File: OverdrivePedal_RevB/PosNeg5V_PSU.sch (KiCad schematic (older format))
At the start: 11 parts, among them U3 TPS60400, U7 SE8233X2, U8 SE8250X2

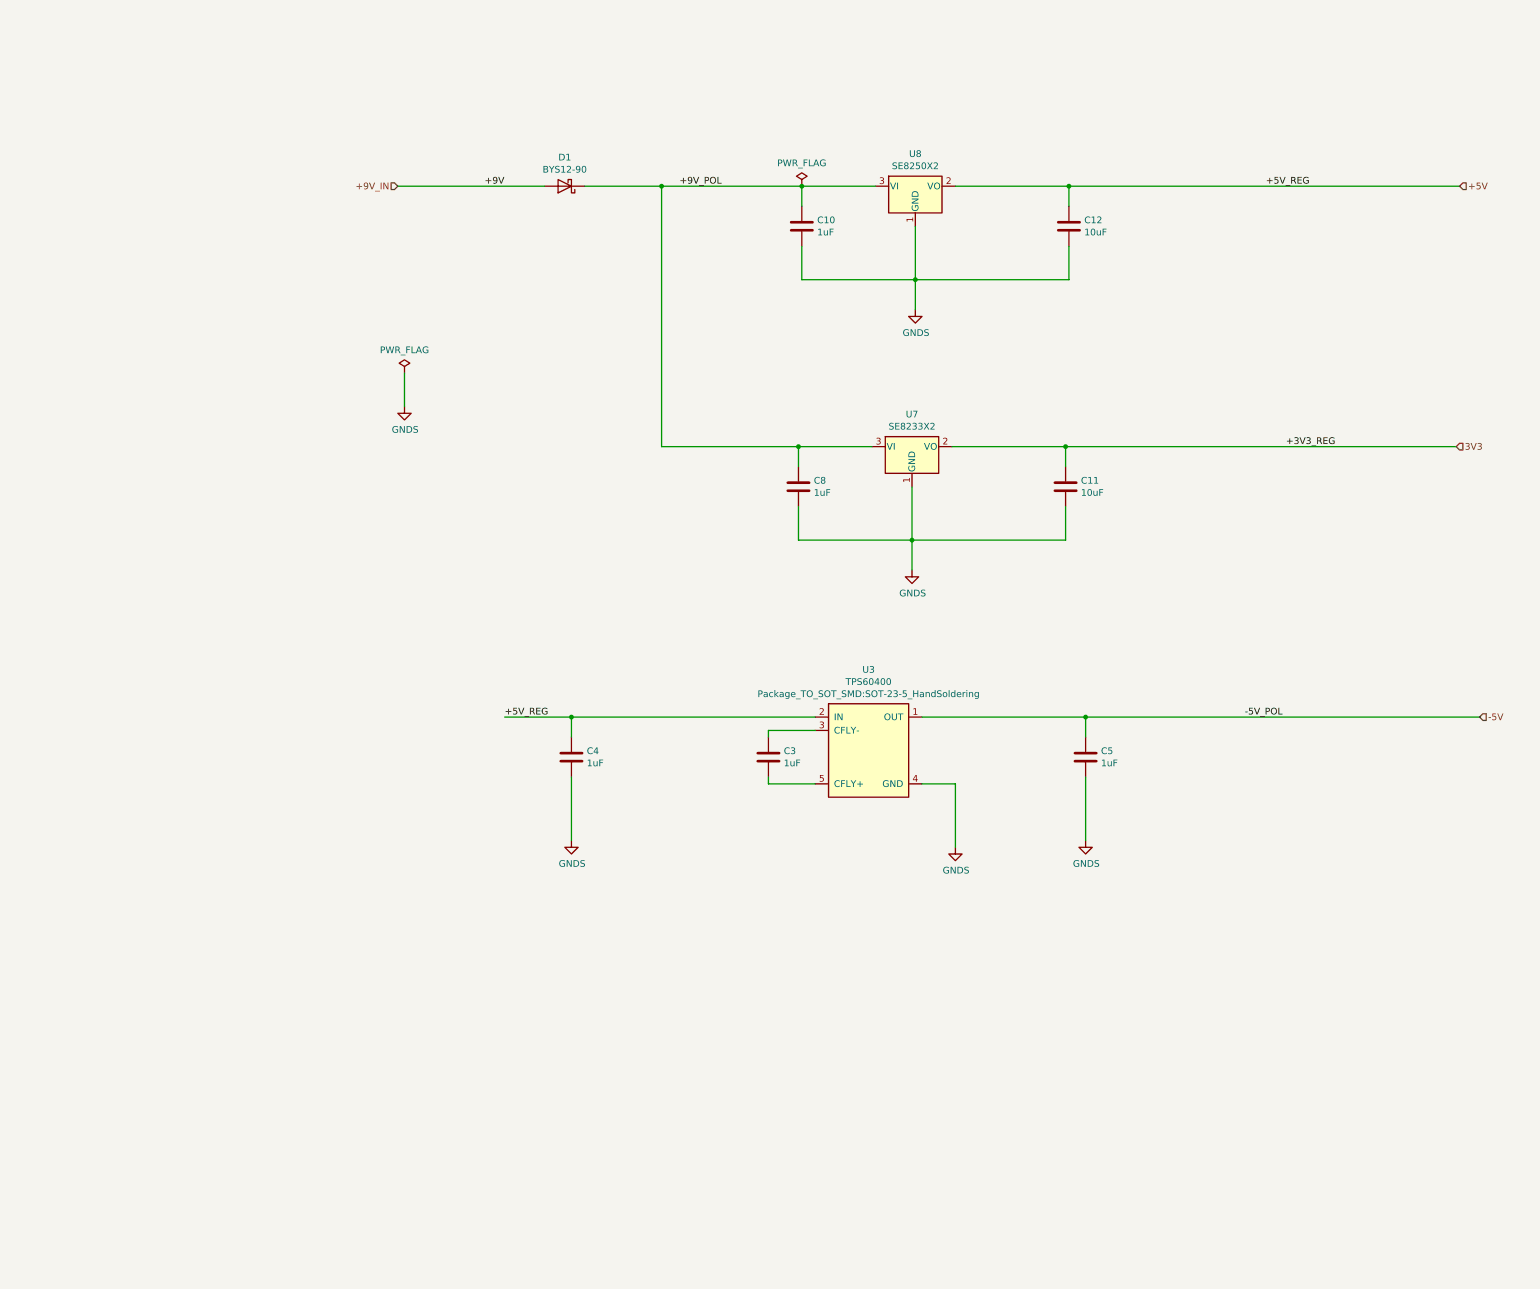
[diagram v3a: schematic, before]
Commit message: Draft layout completed
RevB layout
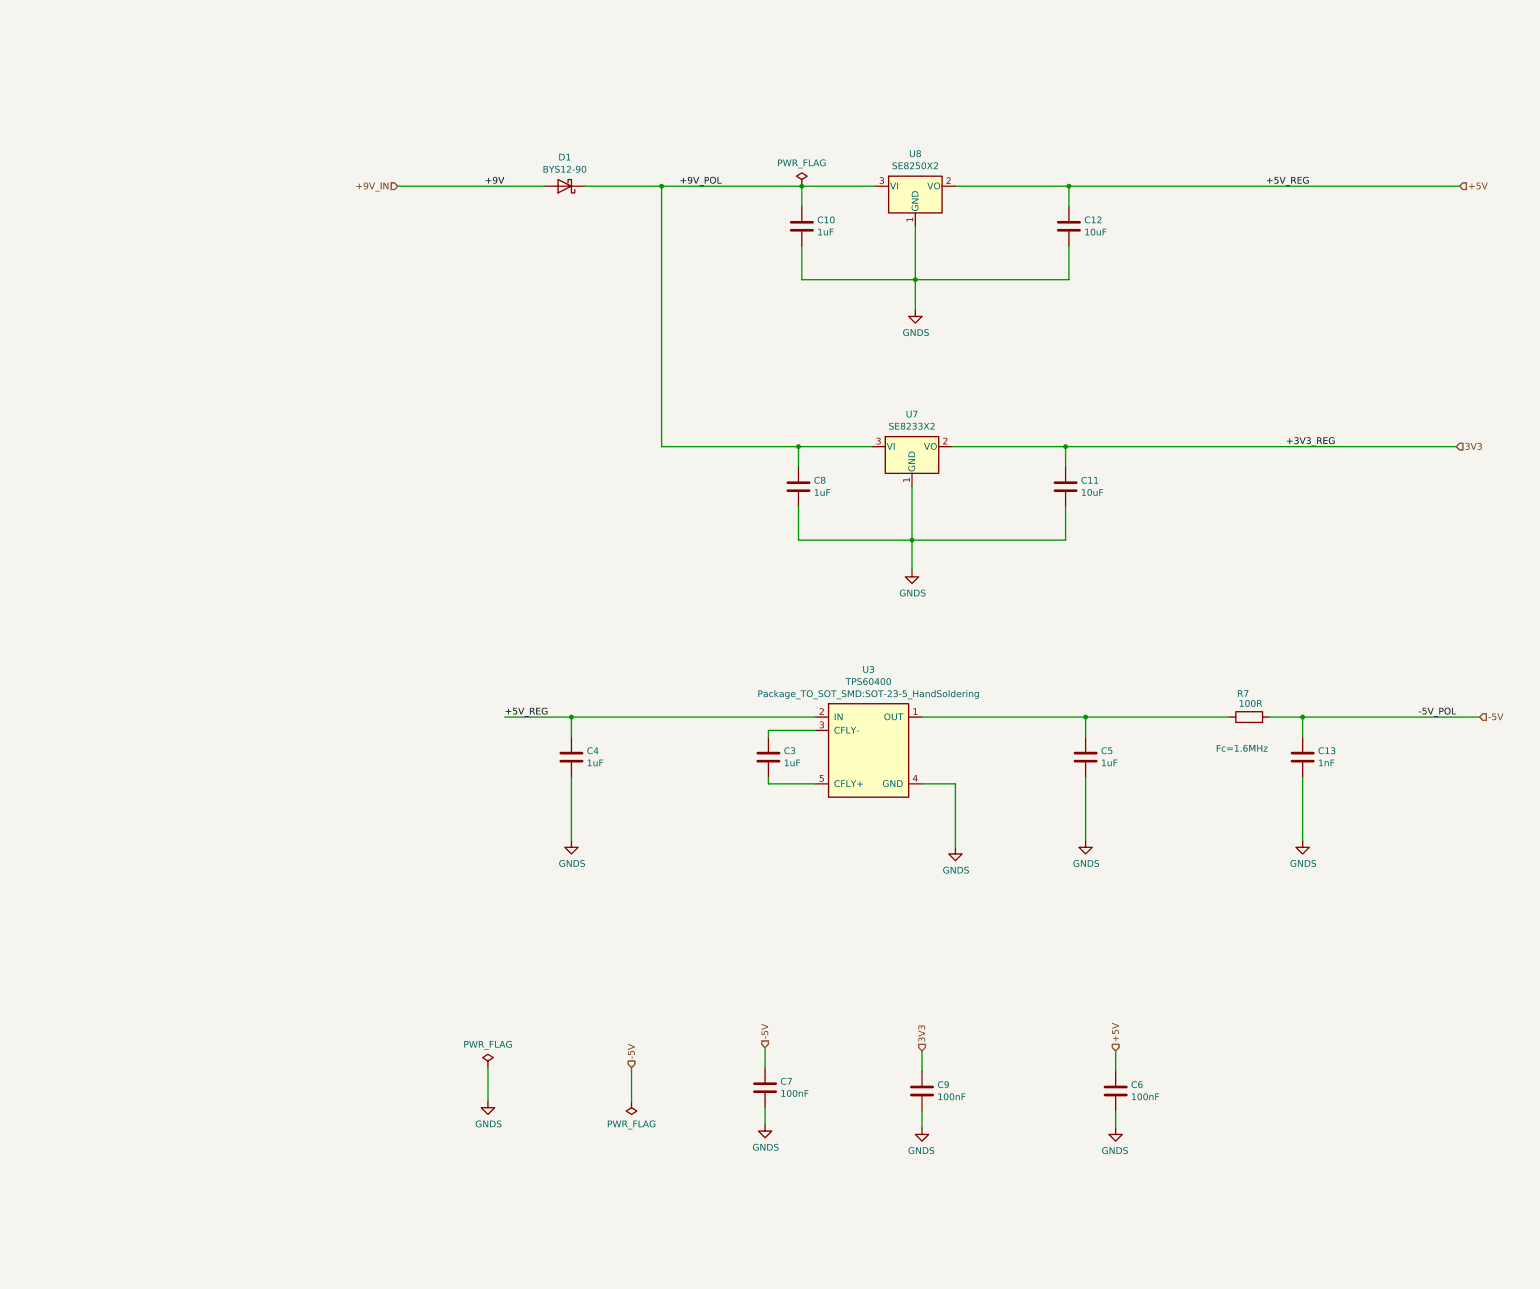
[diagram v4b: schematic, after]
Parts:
- added C13: 1nF, Capacitor_SMD:C_0402_1005Metric, symbol Device:C
- added C6, C7, C9: 100nF, Capacitor_SMD:C_0402_1005Metric, symbol Device:C
- added R7: 100R, Resistor_SMD:R_0402_1005Metric, symbol Device:R
- C10, C11, C12, C3, C4, C5, C8: footprint Capacitor_SMD:C_0805_2012Metric_Pad1.15x1.40mm_HandSolder -> Capacitor_SMD:C_0402_1005Metric
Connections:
- net +5V: now also C6.1
- net -5V: now also C13.1, C7.1, R7.2; no longer C5.1, U3.1 (OUT)
- net 3V3: now also C9.1
- net GNDS: now also C13.2, C6.2, C7.2, C9.2
- new net: C5.1, R7.1, U3.1 (OUT)
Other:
- note added: "Fc=1.6MHz"
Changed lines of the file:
@@
 $Descr A3 16535 11693
 encoding utf-8
-Sheet 2 2
+Sheet 2 3
 Title ""
 Date ""
@@
 F 0 "C3" H 6540 6946 50  0000 L CNN
 F 1 "1uF" H 6540 6855 50  0000 L CNN
-F 2 "Capacitor_SMD:C_0805_2012Metric_Pad1.15x1.40mm_HandSolder" H 6463 6750 50  0001 C CNN
+F 2 "Capacitor_SMD:C_0402_1005Metric" H 6463 6750 50  0001 C CNN
 F 3 "~" H 6425 6900 50  0001 C CNN
 	1    6425 6900
@@
 Text Label 4450 6600 0    50   ~ 0
 +5V_REG
-Text Label 10275 6600 2    50   ~ 0
+Text Label 11575 6600 2    50   ~ 0
 -5V_POL
 Wire Wire Line
@@
 F 0 "C4" H 5065 6946 50  0000 L CNN
 F 1 "1uF" H 5065 6855 50  0000 L CNN
-F 2 "Capacitor_SMD:C_0805_2012Metric_Pad1.15x1.40mm_HandSolder" H 4988 6750 50  0001 C CNN
+F 2 "Capacitor_SMD:C_0402_1005Metric" H 4988 6750 50  0001 C CNN
 F 3 "~" H 4950 6900 50  0001 C CNN
 	1    4950 6900
@@
 F 0 "C5" H 8915 6946 50  0000 L CNN
 F 1 "1uF" H 8915 6855 50  0000 L CNN
-F 2 "Capacitor_SMD:C_0805_2012Metric_Pad1.15x1.40mm_HandSolder" H 8838 6750 50  0001 C CNN
+F 2 "Capacitor_SMD:C_0402_1005Metric" H 8838 6750 50  0001 C CNN
 F 3 "~" H 8800 6900 50  0001 C CNN
 	1    8800 6900
@@
 	8800 7050 8800 7525
 Wire Wire Line
-	8800 6600 11750 6600
+	8800 6600 9875 6600
 Connection ~ 8800 6600
 Text HLabel 11575 4575 2    50   Input ~ 0
@@
 F 0 "C10" H 6790 2971 50  0000 L CNN
 F 1 "1uF" H 6790 2880 50  0000 L CNN
-F 2 "Capacitor_SMD:C_0805_2012Metric_Pad1.15x1.40mm_HandSolder" H 6713 2775 50  0001 C CNN
+F 2 "Capacitor_SMD:C_0402_1005Metric" H 6713 2775 50  0001 C CNN
 F 3 "~" H 6675 2925 50  0001 C CNN
 	1    6675 2925
@@
 F 0 "C12" H 8790 2971 50  0000 L CNN
 F 1 "10uF" H 8790 2880 50  0000 L CNN
-F 2 "Capacitor_SMD:C_0805_2012Metric_Pad1.15x1.40mm_HandSolder" H 8713 2775 50  0001 C CNN
+F 2 "Capacitor_SMD:C_0402_1005Metric" H 8713 2775 50  0001 C CNN
 F 3 "~" H 8675 2925 50  0001 C CNN
 	1    8675 2925
@@
 F 0 "C8" H 6765 4921 50  0000 L CNN
 F 1 "1uF" H 6765 4830 50  0000 L CNN
-F 2 "Capacitor_SMD:C_0805_2012Metric_Pad1.15x1.40mm_HandSolder" H 6688 4725 50  0001 C CNN
+F 2 "Capacitor_SMD:C_0402_1005Metric" H 6688 4725 50  0001 C CNN
 F 3 "~" H 6650 4875 50  0001 C CNN
 	1    6650 4875
@@
 F 0 "C11" H 8765 4921 50  0000 L CNN
 F 1 "10uF" H 8765 4830 50  0000 L CNN
-F 2 "Capacitor_SMD:C_0805_2012Metric_Pad1.15x1.40mm_HandSolder" H 8688 4725 50  0001 C CNN
+F 2 "Capacitor_SMD:C_0402_1005Metric" H 8688 4725 50  0001 C CNN
 F 3 "~" H 8650 4875 50  0001 C CNN
 	1    8650 4875
@@
 L power:PWR_FLAG #FLG0101
 U 1 1 5F1D2B66
-P 3700 4025
-F 0 "#FLG0101" H 3700 4100 50  0001 C CNN
-F 1 "PWR_FLAG" H 3700 4198 50  0000 C CNN
-F 2 "" H 3700 4025 50  0001 C CNN
-F 3 "~" H 3700 4025 50  0001 C CNN
-	1    3700 4025
-	1    0    0    -1
-$EndComp
-Wire Wire Line
-	3700 4025 3700 4275
+P 4325 9225
+F 0 "#FLG0101" H 4325 9300 50  0001 C CNN
+F 1 "PWR_FLAG" H 4325 9398 50  0000 C CNN
+F 2 "" H 4325 9225 50  0001 C CNN
+F 3 "~" H 4325 9225 50  0001 C CNN
+	1    4325 9225
+	1    0    0    -1
+$EndComp
+Wire Wire Line
+	4325 9225 4325 9475
 $Comp
 L power:GNDS #PWR0109
 U 1 1 5F1D3B2E
-P 3700 4275
-F 0 "#PWR0109" H 3700 4025 50  0001 C CNN
-F 1 "GNDS" H 3705 4102 50  0000 C CNN
-F 2 "" H 3700 4275 50  0001 C CNN
-F 3 "" H 3700 4275 50  0001 C CNN
-	1    3700 4275
-	1    0    0    -1
-$EndComp
+P 4325 9475
+F 0 "#PWR0109" H 4325 9225 50  0001 C CNN
+F 1 "GNDS" H 4330 9302 50  0000 C CNN
+F 2 "" H 4325 9475 50  0001 C CNN
+F 3 "" H 4325 9475 50  0001 C CNN
+	1    4325 9475
+	1    0    0    -1
+$EndComp
+$Comp
+L Device:C C13
+U 1 1 5E8237A8
+P 10425 6900
+AR Path="/5E6165F4/5E8237A8" Ref="C13"  Part="1"
+AR Path="/5E6A8284/5E8237A8" Ref="C?"  Part="1"
+F 0 "C13" H 10540 6946 50  0000 L CNN
+F 1 "1nF" H 10540 6855 50  0000 L CNN
+F 2 "Capacitor_SMD:C_0402_1005Metric" H 10463 6750 50  0001 C CNN
+F 3 "~" H 10425 6900 50  0001 C CNN
+	1    10425 6900
+	1    0    0    -1
+$EndComp
+Wire Wire Line
+	10425 6750 10425 6600
+$Comp
+L power:GNDS #PWR035
+U 1 1 5E8237AF
+P 10425 7525
+AR Path="/5E6165F4/5E8237AF" Ref="#PWR035"  Part="1"
+AR Path="/5E6A8284/5E8237AF" Ref="#PWR?"  Part="1"
+F 0 "#PWR035" H 10425 7275 50  0001 C CNN
+F 1 "GNDS" H 10430 7352 50  0000 C CNN
+F 2 "" H 10425 7525 50  0001 C CNN
+F 3 "" H 10425 7525 50  0001 C CNN
+	1    10425 7525
+	1    0    0    -1
+$EndComp
+Wire Wire Line
+	10425 7050 10425 7525
+$Comp
+L Device:R R?
+U 1 1 5E827438
+P 10025 6600
+AR Path="/5E827438" Ref="R?"  Part="1"
+AR Path="/5E6165F4/5E827438" Ref="R7"  Part="1"
+F 0 "R7" V 10200 6600 50  0000 L CNN
+F 1 "100R" V 10125 6500 50  0000 L CNN
+F 2 "Resistor_SMD:R_0402_1005Metric" V 9955 6600 50  0001 C CNN
+F 3 "~" H 10025 6600 50  0001 C CNN
+	1    10025 6600
+	0    -1   -1   0
+$EndComp
+Wire Wire Line
+	10175 6600 10425 6600
+Connection ~ 10425 6600
+Wire Wire Line
+	10425 6600 11750 6600
+Text Notes 9775 6875 0    50   ~ 0
+Fc=1.6MHz
+$Comp
+L Device:C C7
+U 1 1 5EB4CD19
+P 6400 9375
+AR Path="/5E6165F4/5EB4CD19" Ref="C7"  Part="1"
+AR Path="/5E6A8284/5EB4CD19" Ref="C?"  Part="1"
+AR Path="/5EB4CD19" Ref="C?"  Part="1"
+F 0 "C7" H 6515 9421 50  0000 L CNN
+F 1 "100nF" H 6515 9330 50  0000 L CNN
+F 2 "Capacitor_SMD:C_0402_1005Metric" H 6438 9225 50  0001 C CNN
+F 3 "~" H 6400 9375 50  0001 C CNN
+	1    6400 9375
+	1    0    0    -1
+$EndComp
+Wire Wire Line
+	6400 9525 6400 9650
+$Comp
+L power:GNDS #PWR018
+U 1 1 5EB4CD20
+P 6400 9650
+AR Path="/5E6165F4/5EB4CD20" Ref="#PWR018"  Part="1"
+AR Path="/5EB4CD20" Ref="#PWR?"  Part="1"
+F 0 "#PWR018" H 6400 9400 50  0001 C CNN
+F 1 "GNDS" H 6405 9477 50  0000 C CNN
+F 2 "" H 6400 9650 50  0001 C CNN
+F 3 "" H 6400 9650 50  0001 C CNN
+	1    6400 9650
+	1    0    0    -1
+$EndComp
+$Comp
+L Device:C C6
+U 1 1 5EB4CD26
+P 9025 9400
+AR Path="/5E6165F4/5EB4CD26" Ref="C6"  Part="1"
+AR Path="/5E6A8284/5EB4CD26" Ref="C?"  Part="1"
+AR Path="/5EB4CD26" Ref="C?"  Part="1"
+F 0 "C6" H 9140 9446 50  0000 L CNN
+F 1 "100nF" H 9140 9355 50  0000 L CNN
+F 2 "Capacitor_SMD:C_0402_1005Metric" H 9063 9250 50  0001 C CNN
+F 3 "~" H 9025 9400 50  0001 C CNN
+	1    9025 9400
+	1    0    0    -1
+$EndComp
+Wire Wire Line
+	9025 9550 9025 9675
+$Comp
+L power:GNDS #PWR08
+U 1 1 5EB4CD2D
+P 9025 9675
+AR Path="/5E6165F4/5EB4CD2D" Ref="#PWR08"  Part="1"
+AR Path="/5EB4CD2D" Ref="#PWR?"  Part="1"
+F 0 "#PWR08" H 9025 9425 50  0001 C CNN
+F 1 "GNDS" H 9030 9502 50  0000 C CNN
+F 2 "" H 9025 9675 50  0001 C CNN
+F 3 "" H 9025 9675 50  0001 C CNN
+	1    9025 9675
+	-1   0    0    -1
+$EndComp
+Wire Wire Line
+	9025 9100 9025 9250
+Wire Wire Line
+	6400 9075 6400 9225
+$Comp
+L Device:C C9
+U 1 1 5EB4CD35
+P 7575 9400
+AR Path="/5E6165F4/5EB4CD35" Ref="C9"  Part="1"
+AR Path="/5E6A8284/5EB4CD35" Ref="C?"  Part="1"
+AR Path="/5EB4CD35" Ref="C?"  Part="1"
+F 0 "C9" H 7690 9446 50  0000 L CNN
+F 1 "100nF" H 7690 9355 50  0000 L CNN
+F 2 "Capacitor_SMD:C_0402_1005Metric" H 7613 9250 50  0001 C CNN
+F 3 "~" H 7575 9400 50  0001 C CNN
+	1    7575 9400
+	1    0    0    -1
+$EndComp
+Wire Wire Line
+	7575 9550 7575 9675
+$Comp
+L power:GNDS #PWR030
+U 1 1 5EB4CD3C
+P 7575 9675
+AR Path="/5E6165F4/5EB4CD3C" Ref="#PWR030"  Part="1"
+AR Path="/5EB4CD3C" Ref="#PWR?"  Part="1"
+F 0 "#PWR030" H 7575 9425 50  0001 C CNN
+F 1 "GNDS" H 7580 9502 50  0000 C CNN
+F 2 "" H 7575 9675 50  0001 C CNN
+F 3 "" H 7575 9675 50  0001 C CNN
+	1    7575 9675
+	-1   0    0    -1
+$EndComp
+Wire Wire Line
+	7575 9100 7575 9250
+$Comp
+L power:PWR_FLAG #FLG0103
+U 1 1 5EB92E62
+P 5400 9475
+F 0 "#FLG0103" H 5400 9550 50  0001 C CNN
+F 1 "PWR_FLAG" H 5400 9648 50  0000 C CNN
+F 2 "" H 5400 9475 50  0001 C CNN
+F 3 "~" H 5400 9475 50  0001 C CNN
+	1    5400 9475
+	-1   0    0    1
+$EndComp
+Wire Wire Line
+	5400 9475 5400 9225
+Text HLabel 6400 9075 1    50   Input ~ 0
+-5V
+Text HLabel 7575 9100 1    50   Input ~ 0
+3V3
+Text HLabel 9025 9100 1    50   Input ~ 0
++5V
+Text HLabel 5400 9225 1    50   Input ~ 0
+-5V
 $EndSCHEMATC

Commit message: updated draft
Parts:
- added C16, C18, C19: 1uF, Capacitor_SMD:C_0402_1005Metric, symbol Device:C
- added C20: 1nF, Capacitor_SMD:C_0402_1005Metric, symbol Device:C
- added R5: 100R, Resistor_SMD:R_0402_1005Metric, symbol Device:R
- added TP5, TP6, TP7: TestPoint, TestPoint:TestPoint_Pad_1.0x1.0mm, symbol Connector:TestPoint
- added U11: TPS60400, Package_TO_SOT_SMD:SOT-23-5_HandSoldering, symbol TPS6040x:TPS60400
- C10, C8: footprint Capacitor_SMD:C_0402_1005Metric -> Capacitor_SMD:C_0805_2012Metric_Pad1.15x1.40mm_HandSolder
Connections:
- net +5V: now also C16.1, TP5.1, U11.2 (IN)
- net -5V: now also C20.1, R5.2, TP7.1
- net 3V3: now also TP6.1
- net GNDS: now also C16.2, C19.2, C20.2, U11.4 (GND)
- new net: C18.1, U11.3 (CFLY-)
- new net: C18.2, U11.5 (CFLY+)
- new net: C19.1, R5.1, U11.1 (OUT)
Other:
- moved on the sheet: C10, C11, C12, C13, C3, C4, C5, C6, C7, C8, C9, D1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
